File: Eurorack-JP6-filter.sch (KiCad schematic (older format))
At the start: 145 parts, among them J1 JACK_MONO_SW, J2 JACK_MONO_SW, J3 JACK_MONO_SW, J4 JACK_MONO_SW, J5 JACK_MONO_SW, J6 JACK_MONO_SW, P1 CONN_02X05, Q1 BCM857BS, Q2 BCM857BS, Q3 J112, Q4 J112, Q5 J112, Q6 J112, SW1 KS-01Q, U1 TL072-, U10 CD4027, U11 CD40106, U2 TL072-, U3 TL072-, U4 TL072-, U5 LM13700, U6 LM13700, U7 LM13700, U8 DG409, U9 CD4052

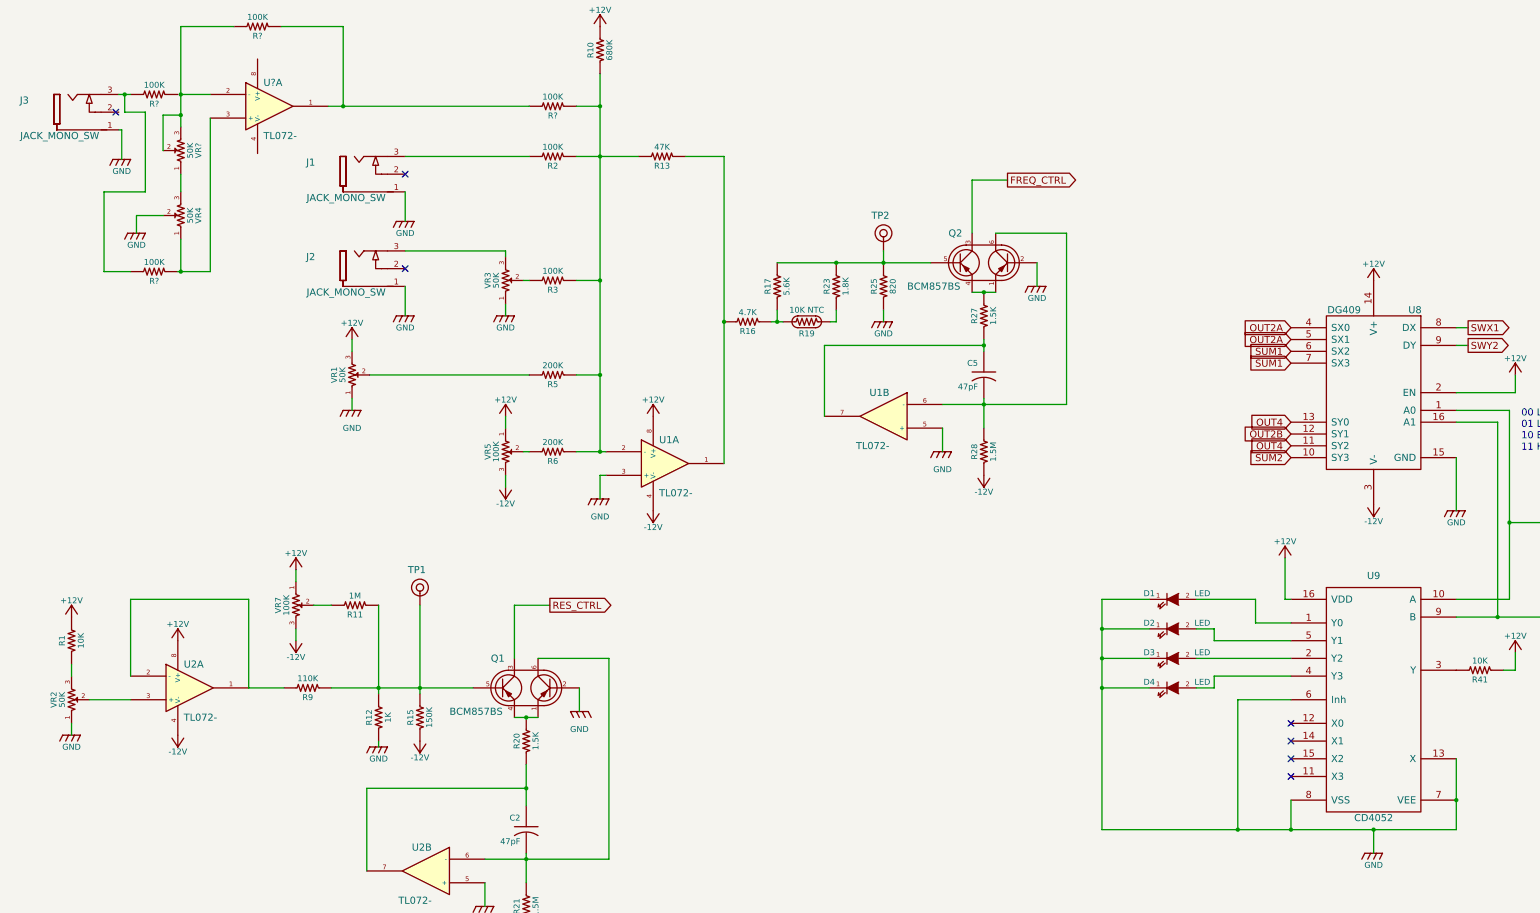
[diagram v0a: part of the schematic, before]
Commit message: added resonance CV input
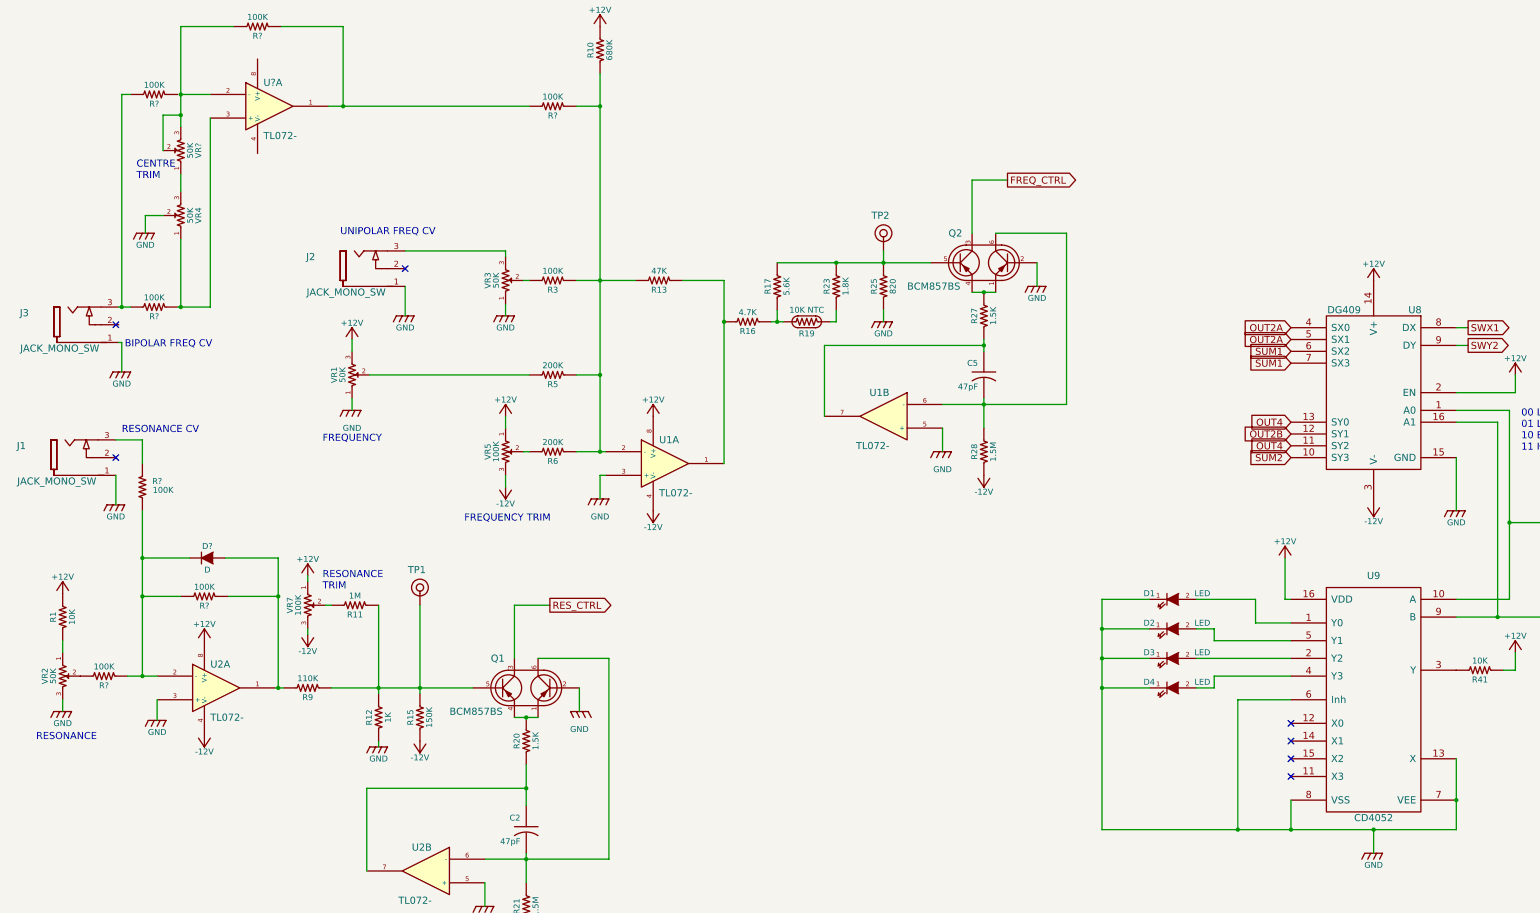
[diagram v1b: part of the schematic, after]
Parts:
- removed R2: 100K, MyModules:SM0603-R-JRL, symbol R_US
- added D?: D, symbol D
- added R? (x3): 100K, MyModules:SM0603-R-JRL, symbol R_US
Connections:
- net GND: now also U2.3 (+), VR2.3; no longer VR2.1
- net at R9.2, U2.1: now also D?.2 (A), R?.1; no longer U2.2 (-)
- net at VR2.2: now also R?.2; no longer U2.3 (+)
- net at R1.2: now also VR2.1; no longer VR2.3
- net at J1.3: now also R?.2
- new net: D?.1 (K), R?.1, R?.1, R?.2, U2.2 (-)
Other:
- note added: "BIPOLAR FREQ CV"
- note added: "CENTRE\nTRIM"
- note added: "FREQUENCY"
- note added: "FREQUENCY TRIM"
- note added: "RESONANCE"
- note added: "RESONANCE CV"
- note added: "RESONANCE\nTRIM"
- note added: "UNIPOLAR FREQ CV"
- moved on the sheet: J1, J3, R1, R13, R?, U2A, VR2, VR7

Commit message: needed to ad inverting stage to resonance jack input so more positive CV = more resonance. Question: is diode clamp required on resonance CV jack input?
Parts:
- removed D?: D, symbol D
- added D?: 1N914, MyModules:SOD323-C1A2, symbol D
- added R? (x2): 100K, MyModules:SM0603-R-JRL, symbol R_US
- added U?: TL072-, MyModules:TSSOP8-JRL, symbol TL072-
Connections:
- net GND: now also U?.3 (+)
- net at R?.1, R?.2, U2.2 (-): now also R?.2; no longer R?.1
- net at R?.2, U?.2 (-), VR?.2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: now also R?.1
- new net: D?.1 (K), R?.1, R?.2, U?.2 (-)
- new net: D?.2 (A), R?.1, R?.1, U?.1
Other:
- note added: "Is clamping diode needed?"
- moved on the sheet: C1, C12, C13, C14, C15, C16, C17, C18, C19, C2, C20, C21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
